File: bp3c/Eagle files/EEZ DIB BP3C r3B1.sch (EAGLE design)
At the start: 58 parts, among them IC1 TCA9534PWR, Q1 2N7002, Q2 2N7002, Q3 2N7002, Q4 2N7002, X1 ZL202-20G, X2 ZL202-20G, X3 ZL202-20G, X4 ZL212-40KG, X5 ZL262-28DG, X6 ZL262-28DG, X7 ZL262-28DG, X8 N.C.

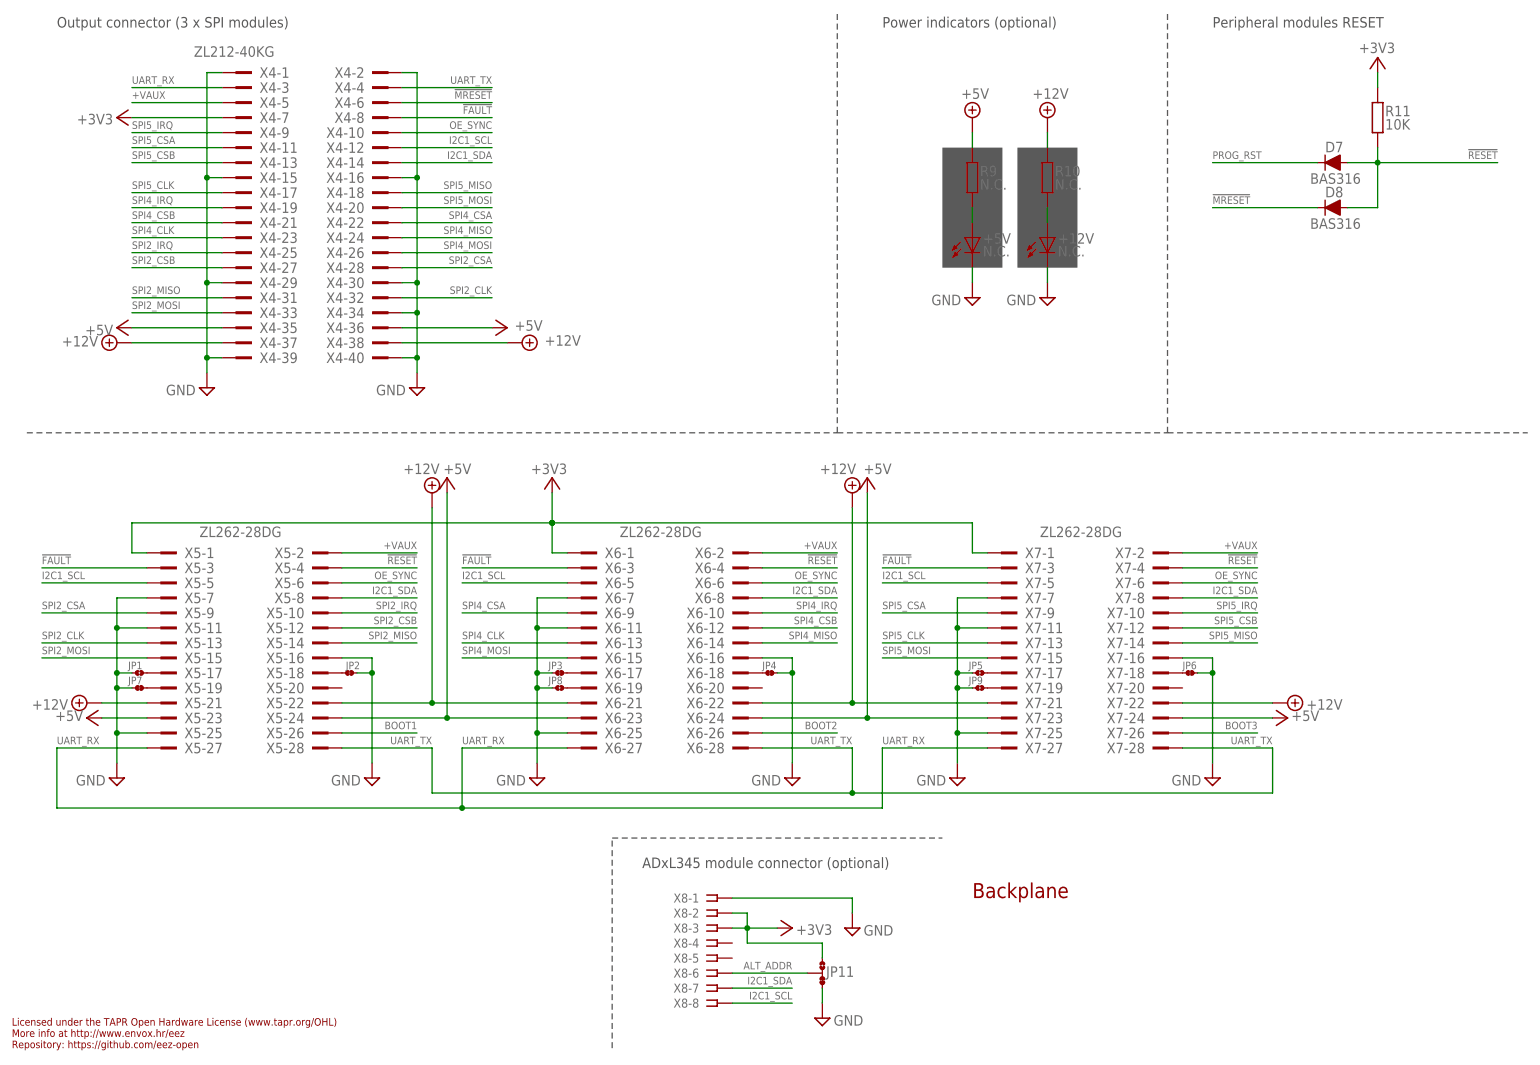
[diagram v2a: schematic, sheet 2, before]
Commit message: update TME connectors in BOMs
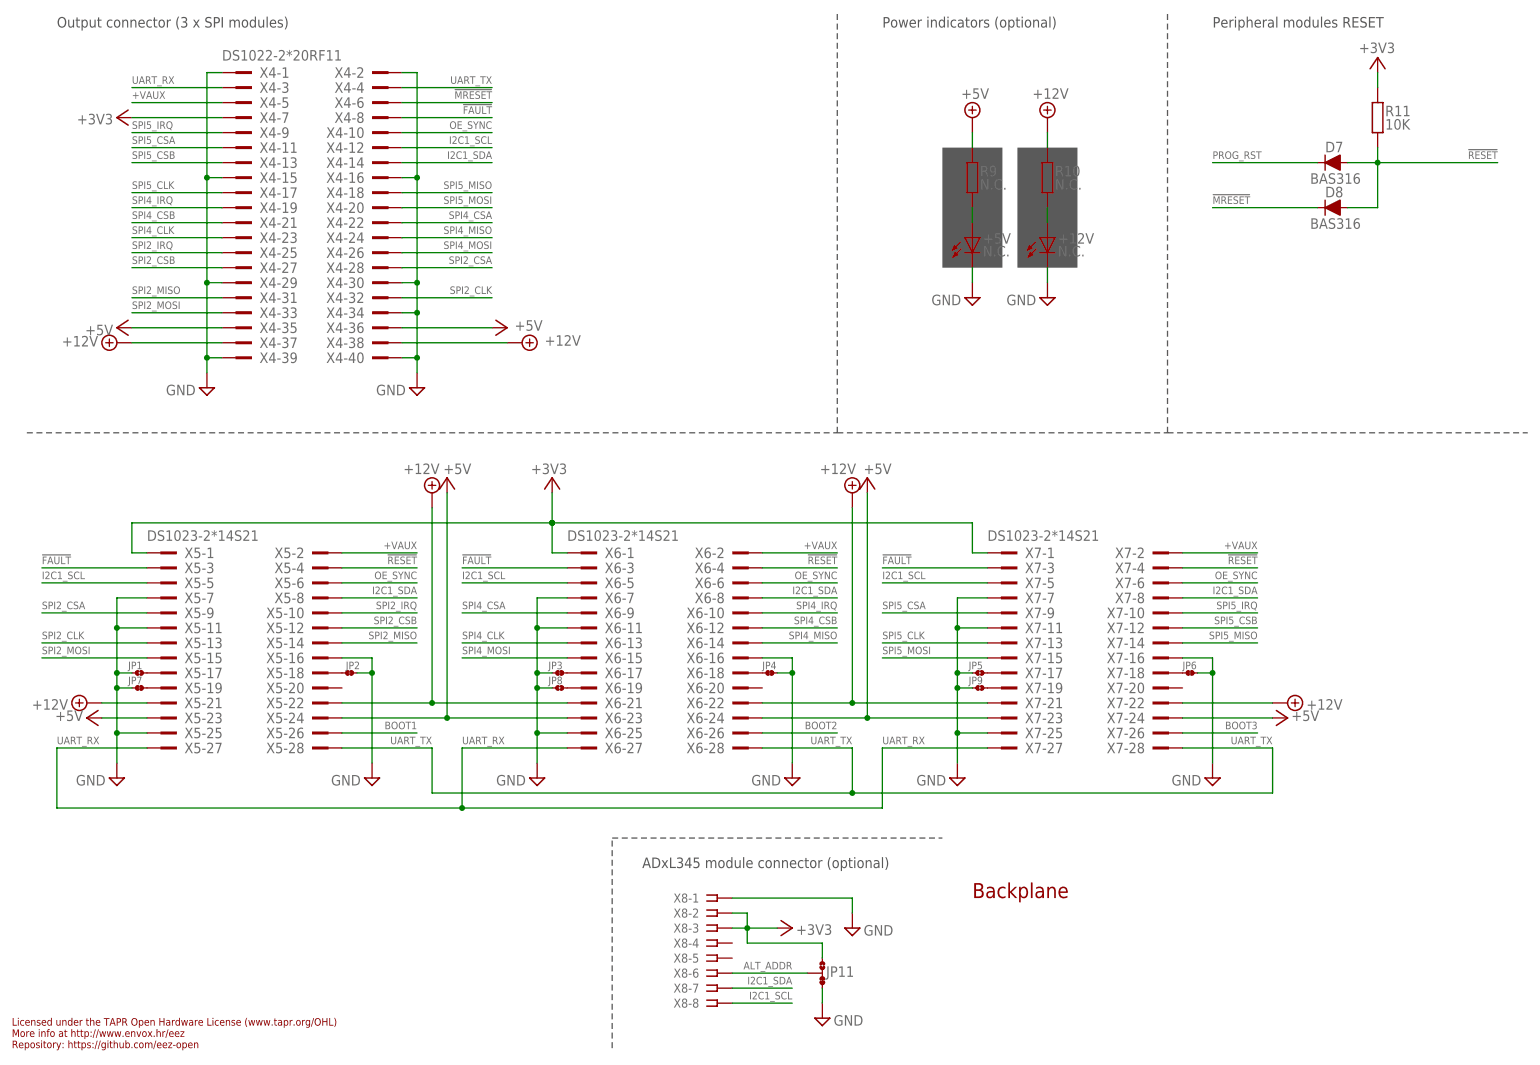
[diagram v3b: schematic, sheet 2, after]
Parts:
- X4: value ZL212-40KG -> DS1022-2*20RF11
- X5, X6, X7: value ZL262-28DG -> DS1023-2*14S21
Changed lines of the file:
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@@
 <setting verticaltext="up"/>
 </settings>
-<grid distance="0.1" unitdist="inch" unit="inch" style="lines" multiple="1" display="no" altdistance="0.01" altunitdist="inch" altunit="inch"/>
+<grid distance="0.025" unitdist="inch" unit="inch" style="lines" multiple="4" display="no" altdistance="0.01" altunitdist="inch" altunit="inch"/>
 <layers>
 <layer number="1" name="Top" color="4" fill="1" visible="no" active="no"/>
@@
 <part name="X2" library="EEZ_connectors" deviceset="DS1021-2*10SF11" device="" value="ZL202-20G"/>
 <part name="X3" library="EEZ_connectors" deviceset="DS1021-2*10SF11" device="" value="ZL202-20G"/>
-<part name="X4" library="EEZ_connectors" deviceset="ZL212-40KG" device=""/>
+<part name="X4" library="EEZ_connectors" deviceset="ZL212-40KG" device="" value="DS1022-2*20RF11"/>
 <part name="+5V" library="EEZ_Lib1" deviceset="LED" device="0805" value="N.C."/>
 <part name="R9" library="rcl" deviceset="R-EU_" device="R0805" value="N.C."/>
@@
 <part name="D4" library="EEZ_Lib1" deviceset="DIODE" device="SOD323R" value="N.C."/>
 <part name="D3" library="EEZ_Lib1" deviceset="DIODE" device="SOD323R" value="N.C."/>
-<part name="X5" library="EEZ_connectors" deviceset="TSW-114-07-F-D" device="" value="ZL262-28DG"/>
-<part name="X6" library="EEZ_connectors" deviceset="TSW-114-07-F-D" device="" value="ZL262-28DG"/>
-<part name="X7" library="EEZ_connectors" deviceset="TSW-114-07-F-D" device="" value="ZL262-28DG"/>
+<part name="X5" library="EEZ_connectors" deviceset="TSW-114-07-F-D" device="" value="DS1023-2*14S21"/>
+<part name="X6" library="EEZ_connectors" deviceset="TSW-114-07-F-D" device="" value="DS1023-2*14S21"/>
+<part name="X7" library="EEZ_connectors" deviceset="TSW-114-07-F-D" device="" value="DS1023-2*14S21"/>
 <part name="JP10" library="EEZ_Lib1" deviceset="JP3-CUT" device=""/>
 <part name="D7" library="EEZ_Lib1" deviceset="DIODE" device="SOD323R" value="BAS316"/>
@@
 <instance part="X4" gate="-1" x="38.1" y="167.64" smashed="yes" rot="MR0">
 <attribute name="NAME" x="44.45" y="168.529" size="1.778" layer="95" rot="MR180"/>
-<attribute name="VALUE" x="46.99" y="170.307" size="1.778" layer="96" rot="MR0"/>
+<attribute name="VALUE" x="38.1" y="169.672" size="1.778" layer="96"/>
 </instance>
 <instance part="SUPPLY4" gate="+12V" x="73.66" y="96.52" smashed="yes">
@@
 <instance part="X5" gate="-1" x="25.4" y="86.36" smashed="yes" rot="MR0">
 <attribute name="NAME" x="31.75" y="87.249" size="1.778" layer="95" rot="MR180"/>
-<attribute name="VALUE" x="34.29" y="89.027" size="1.778" layer="96"/>
+<attribute name="VALUE" x="25.4" y="88.392" size="1.778" layer="96"/>
 </instance>
 <instance part="X5" gate="-2" x="58.42" y="86.36" smashed="yes">
@@
 <instance part="X6" gate="-1" x="96.52" y="86.36" smashed="yes" rot="MR0">
 <attribute name="NAME" x="102.87" y="87.249" size="1.778" layer="95" rot="MR180"/>
-<attribute name="VALUE" x="105.41" y="89.027" size="1.778" layer="96"/>
+<attribute name="VALUE" x="96.52" y="88.392" size="1.778" layer="96"/>
 </instance>
 <instance part="X6" gate="-2" x="129.54" y="86.36"/>
@@
 <instance part="X7" gate="-1" x="167.64" y="86.36" smashed="yes" rot="MR0">
 <attribute name="NAME" x="173.99" y="87.249" size="1.778" layer="95" rot="MR180"/>
-<attribute name="VALUE" x="176.53" y="89.027" size="1.778" layer="96"/>
+<attribute name="VALUE" x="167.64" y="88.392" size="1.778" layer="96"/>
 </instance>
 <instance part="X7" gate="-2" x="200.66" y="86.36"/>
